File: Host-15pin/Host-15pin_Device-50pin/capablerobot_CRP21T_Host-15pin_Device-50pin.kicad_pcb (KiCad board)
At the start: 2 copper layers, 25.5 x 99.8 mm, 2 parts, among them J1 WE_686715100001_FLEX, J2 WE_687650100002_FLEX

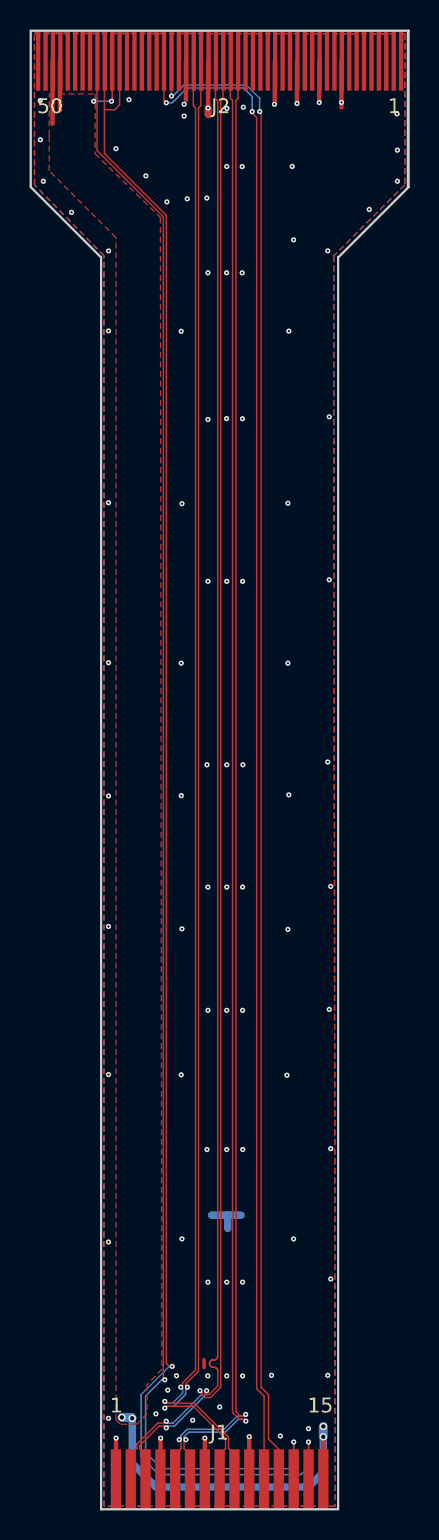
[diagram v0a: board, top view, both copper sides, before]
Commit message: Change 22 pin to 4 lane interface and change 15 pin and 22 pin to alternate MIPI interface
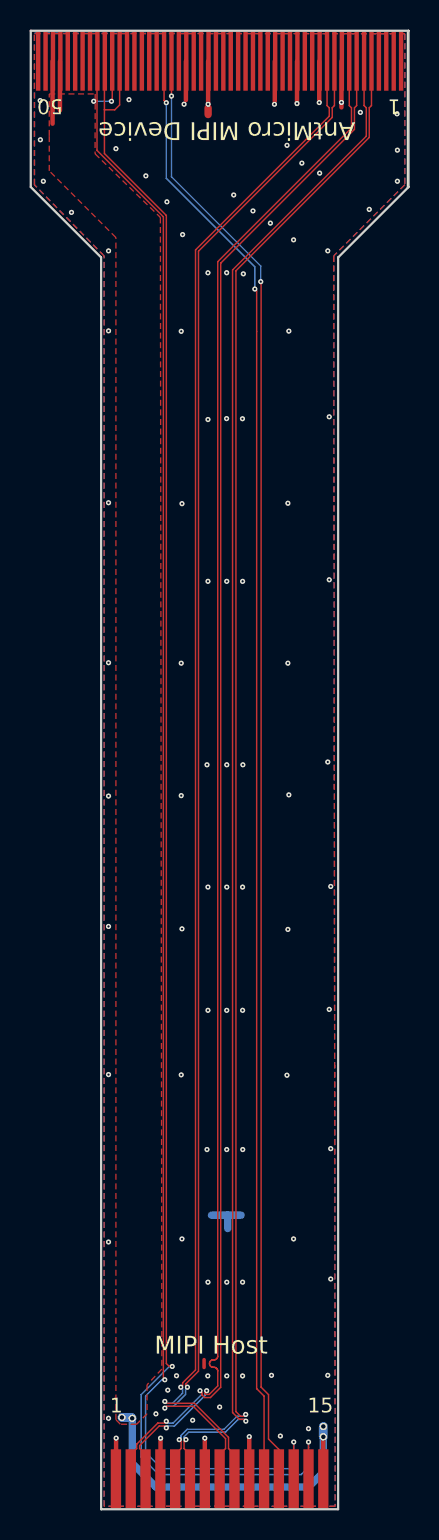
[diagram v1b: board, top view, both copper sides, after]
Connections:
- J2 pad 1: Net-(J2-Pad1) -> (no net)
- J2 pad 10: Net-(J2-Pad10) -> /CSI0_CLK_N
- J2 pad 11: Net-(J2-Pad11) -> /CSI0_CLK_P
- J2 pad 13: Net-(J2-Pad13) -> (no net)
- J2 pad 14: Net-(J2-Pad14) -> (no net)
- J2 pad 16: Net-(J2-Pad16) -> (no net)
- J2 pad 17: Net-(J2-Pad17) -> (no net)
- J2 pad 19: Net-(J2-Pad19) -> (no net)
- J2 pad 2: Net-(J2-Pad2) -> (no net)
- J2 pad 20: Net-(J2-Pad20) -> (no net)
- J2 pad 21: Net-(J2-Pad21) -> (no net)
- J2 pad 22: Net-(J2-Pad22) -> (no net)
- J2 pad 23: /CSI0_D1_N -> (no net)
- J2 pad 24: /CSI0_D1_P -> (no net)
- J2 pad 25: /CSI0_D0_N -> (no net)
- J2 pad 26: /CSI0_D0_P -> (no net)
- J2 pad 28: /CSI0_CLK_N -> (no net)
- J2 pad 29: /CSI0_CLK_P -> (no net)
- J2 pad 3: Net-(J2-Pad3) -> (no net)
- J2 pad 31: Net-(J2-Pad31) -> (no net)
- J2 pad 34: Net-(J2-Pad34) -> (no net)
- J2 pad 35: Net-(J2-Pad35) -> (no net)
- J2 pad 36: Net-(J2-Pad36) -> (no net)
- J2 pad 37: Net-(J2-Pad37) -> (no net)
- J2 pad 38: Net-(J2-Pad38) -> (no net)
- J2 pad 4: Net-(J2-Pad4) -> (no net)
- J2 pad 43: Net-(J2-Pad43) -> (no net)
- J2 pad 44: Net-(J2-Pad44) -> (no net)
- J2 pad 45: Net-(J2-Pad45) -> (no net)
- J2 pad 46: Net-(J2-Pad46) -> (no net)
- J2 pad 49: Net-(J2-Pad49) -> (no net)
- J2 pad 5: Net-(J2-Pad5) -> /CSI0_D1_N
- J2 pad 50: Net-(J2-Pad50) -> (no net)
- J2 pad 6: Net-(J2-Pad6) -> /CSI0_D1_P
- J2 pad 7: Net-(J2-Pad7) -> /CSI0_D0_N
- J2 pad 8: Net-(J2-Pad8) -> /CSI0_D0_P
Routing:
- net /RST: track 103.0 -> 98.5 mm
- net /IO1: track 102.7 -> 98.8 mm
- net /CSI0_D0_P: track 100.3 -> 104.0 mm
- net /CSI0_D1_P: track 100.2 -> 104.0 mm
- net /CSI0_CLK_P: track 100.3 -> 104.0 mm
- net /CSI0_D0_N: track 100.3 -> 104.0 mm
- net /CSI0_CLK_N: track 100.3 -> 104.0 mm
- net /CSI0_D1_N: track 100.2 -> 103.9 mm
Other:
- board text added: "AntMicro MIPI Device"
- board text added: "Capable Robot Components Inc [CRP21T.1] Flex Cable - CSI - 15 pin Host to 50 pin Device 100mm, same side contacts"
- board text added: "MIPI Host"
- board text removed: "Capable Robot Components Inc [CRP21T] Flex Cable - CSI - 50 pin Device to 15 pin Host 100mm, same side contacts"
